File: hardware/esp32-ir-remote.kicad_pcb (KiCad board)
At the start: 2 copper layers, 92 x 44 mm, 57 parts, among them J2 USB_C_Receptacle_USB2.0_14P, J4 GPIO_PWR, J5 EXT_IR, Q3 AO3400A, SW1 RESET, SW2 BOOT, U1 AMS1117-3.3, U3 ESP32-C3-WROOM-02, U4 TSOP382xx, U5 AHT20

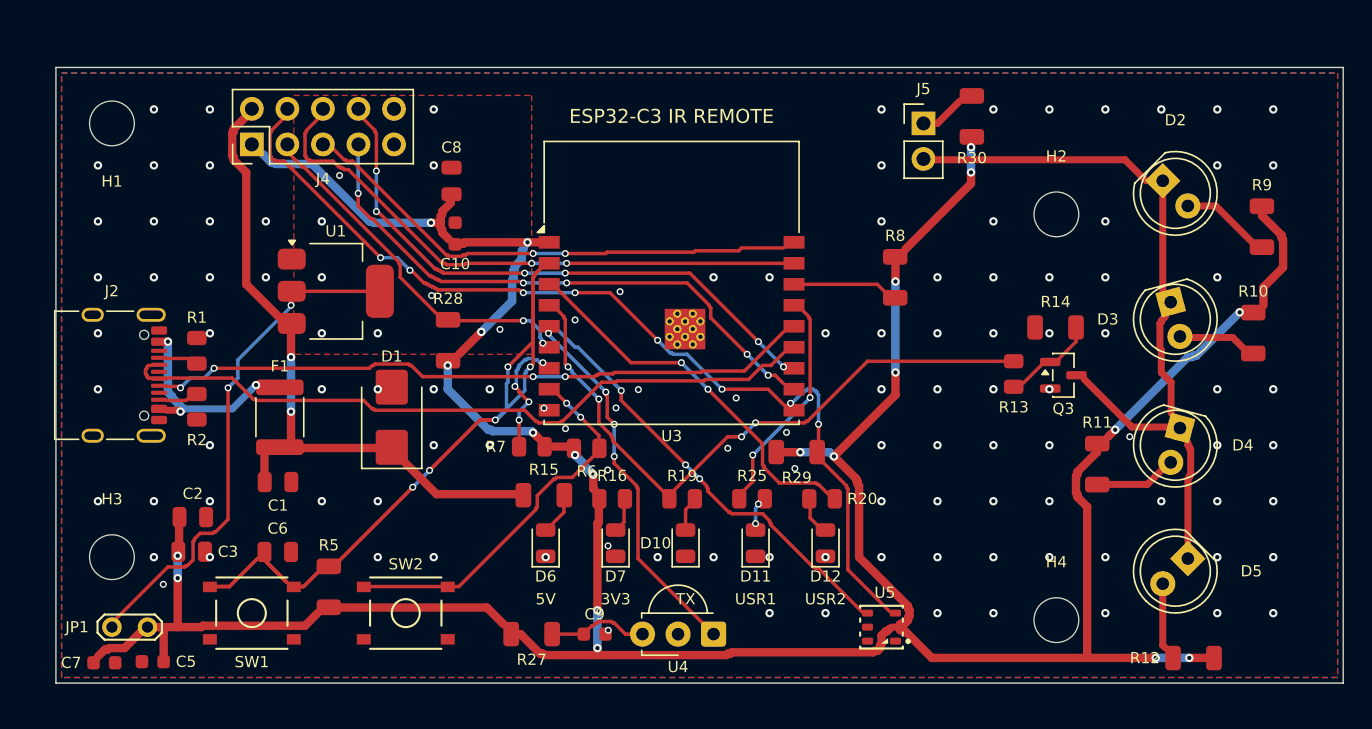
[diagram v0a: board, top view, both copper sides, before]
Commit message: fix(pcb): SI re-layout — USB pair + receiver off the ground plane
Full re-layout pass (Nick's call) resolving the review's SI findings, with
the hand-tuned anchors fixed so the IR fan + U4 south-edge relocation are
preserved (synced into pcb_floorplan.py). Router taught real SI rules:

- pcb_router HARD_F: USB D+/D- forbidden from B.Cu -> both 100% F.Cu, 0 vias,
  no plane crossing (was D+ 5.3mm on B.Cu + 4 vias). SI-critical nets routed
  first so they get clean paths; the USB-C A6<->B6 tie now routes too.
- pcb_router STRONG_F: IR_RX 5.5->2.7mm single crossing; IR_RX_VS 0mm on B.Cu.
- pcb_ldo_pour: /LDO_OUT tab thermal copper ~20 -> ~69mm2.

Result vs committed board (validated on KiCad 10.0.3, libs wired):
  DRC 0 errors; unconnected 1->0; silk_overlap 44->0; silk_over_copper 53->0;
  all 36 multi-pad nets routed; anchors preserved. Baseline refreshed.

Decoupling left ~7mm (bounded by the WROOM module courtyard; module has
internal decoupling). FS-USB skew 12.7mm is electrically irrelevant.
Baseline made on 10.0.3 vs CI's 10.0.2 - watch the first CI run.

https://claude.ai/code/session_012MXcXwLmTqFYpQEkNAaPpq
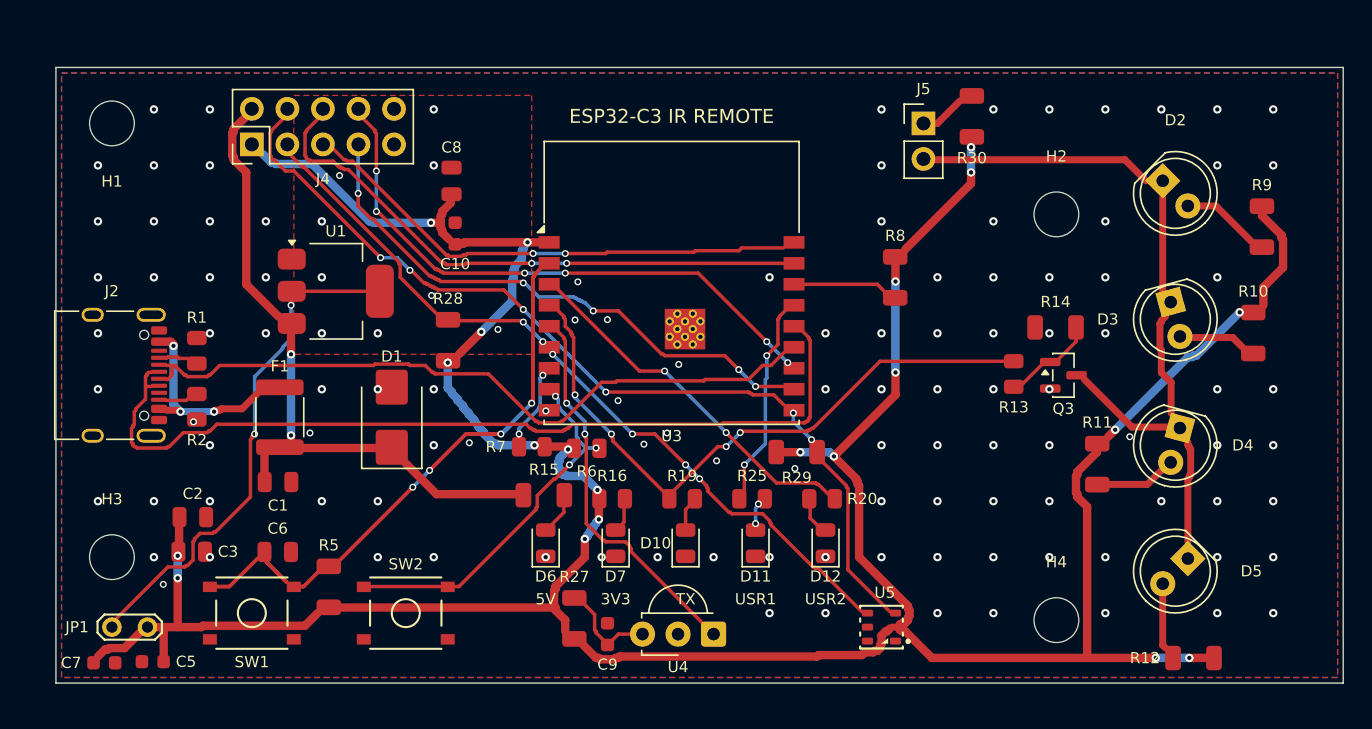
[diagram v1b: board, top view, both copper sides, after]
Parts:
- moved R27 3.25 mm to (143.1, 109.4), turned to 90 degrees
- moved C9 0.92 mm to (145.4, 110.5), turned to 90 degrees
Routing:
- net /USB_D+: track 46.5 -> 62.5 mm, vias 4 -> 0
- net /I2C_SCL: track 65.9 -> 62.3 mm, vias 8 -> 6
- net /IO8_STRAP: track 8.06 -> 5.30 mm, vias 4 -> 2
- net /I2C_SDA: track 55.2 -> 52.4 mm, vias 5 -> 6
- net /ESP_EN: track 70.1 -> 71.8 mm, vias 5 -> 4
- net +3.3V: track 225.5 -> 226.6 mm
- net /USER_LED1: track 15.0 -> 14.0 mm
- net /USER_LED2: track 26.3 -> 25.3 mm
- net /ESP_BOOT: track 23.9 -> 24.6 mm, vias 2 -> 3
- net /IR_RX: track 25.4 -> 25.9 mm, vias 4 -> 2
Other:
- board text added: "2026-06-14 git 68e2410-dirty"
- board text removed: "2026-06-14 git b1f41e0-dirty"

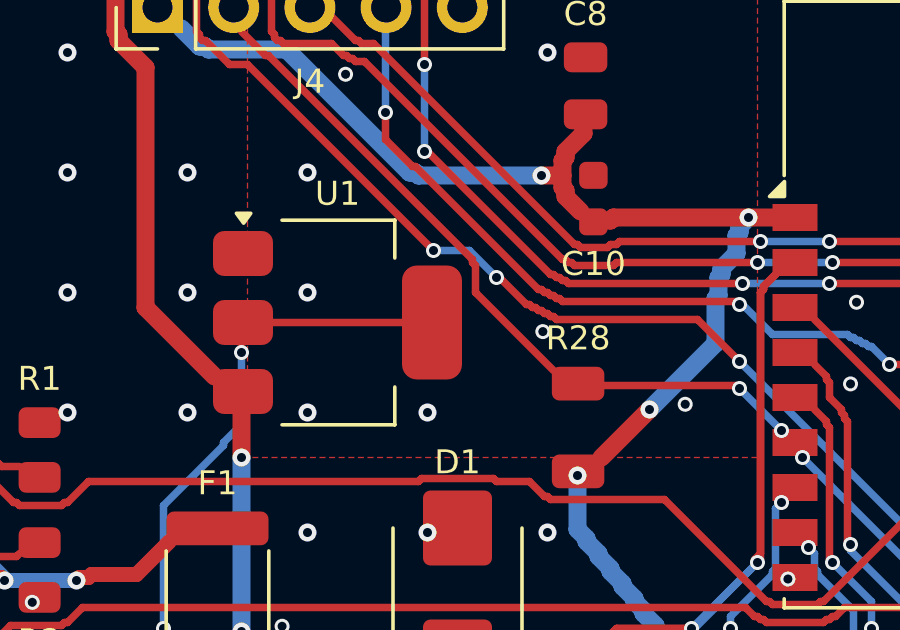
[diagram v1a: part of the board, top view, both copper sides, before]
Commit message: fix(pcb): two-sided LDO thermal stack — B.Cu island + thermal vias
The top-only 68.5 mm2 /LDO_OUT pour left no worst-case margin (T_J ~120 C at
the 0.85 W rated load). pcb_ldo_pour.py now also lays a B.Cu /LDO_OUT island
(43.8 mm2) hugging the tab plus a 2x3 array of thermal vias (0.3/0.6 mm) that
tie the top tab/pour straight through the FR-4 to the bottom island
(~112 mm2 two-sided). The island is kept tight to the tab so the B.Cu ground
plane is only slotted in the west power zone, away from the IR_RX/USB returns.

theta_JA est. ~110 -> ~90 C/W => T_J ~120 -> ~101 C at 25 C ambient (24 C
margin), ~116 C in a 40 C enclosure: now under the 125 C limit at the rated
load. Still short of the 1-in2 ideal (the dense power zone caps the island
size); relocating U1 to open copper is the remaining lever.

Validated on KiCad 10.0.3 in-container: kicad-cli pcb drc 0 violations /
0 unconnected; hardware_validate.py all checks pass, no baseline drift.

https://claude.ai/code/session_01WvC98kUxrLszJZvcojTJeU
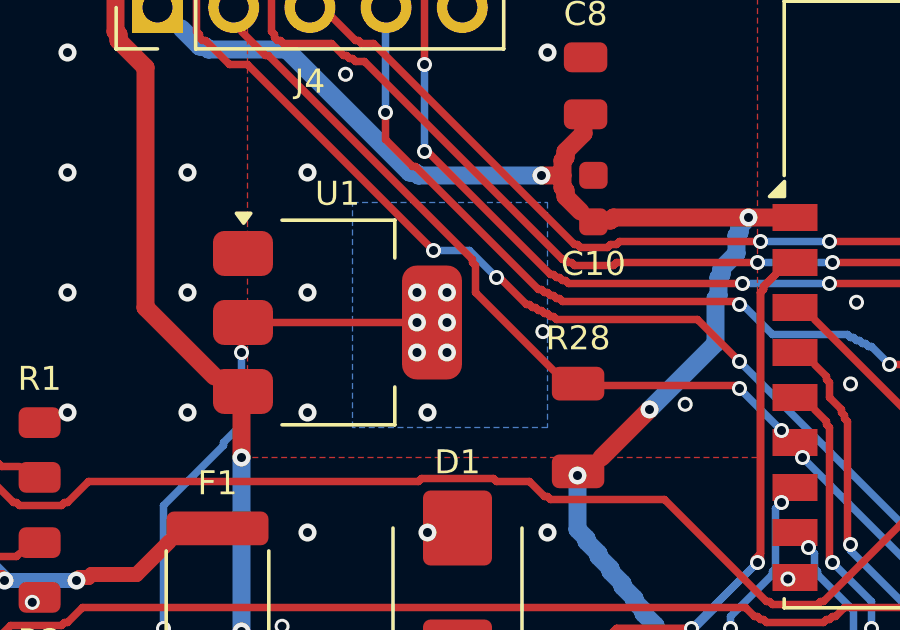
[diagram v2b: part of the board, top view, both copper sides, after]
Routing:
- net /LDO_OUT: vias 2 -> 8
- added copper zone on B.Cu, net /LDO_OUT
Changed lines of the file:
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@@
+	)
+	(via
+		(at 129.65 87)
+		(size 0.6)
+		(drill 0.3)
+		(layers "F.Cu" "B.Cu")
+		(net "/LDO_OUT")
+	)
+	(via
+		(at 128.65 87)
+		(size 0.6)
+		(drill 0.3)
+		(layers "F.Cu" "B.Cu")
+		(net "/LDO_OUT")
 	)
 	(via
@@
 	)
 	(via
+		(at 128.65 86)
+		(size 0.6)
+		(drill 0.3)
+		(layers "F.Cu" "B.Cu")
+		(net "/LDO_OUT")
+	)
+	(via
+		(at 128.65 85)
+		(size 0.6)
+		(drill 0.3)
+		(layers "F.Cu" "B.Cu")
+		(net "/LDO_OUT")
+	)
+	(via
+		(at 129.65 85)
+		(size 0.6)
+		(drill 0.3)
+		(layers "F.Cu" "B.Cu")
+		(net "/LDO_OUT")
+	)
+	(via
 		(at 120.2 96.2)
 		(size 0.5)
+		(drill 0.3)
+		(layers "F.Cu" "B.Cu")
+		(net "/LDO_OUT")
+	)
+	(via
+		(at 129.65 86)
+		(size 0.6)
 		(drill 0.3)
 		(layers "F.Cu" "B.Cu")
@@
 		(layer "F.Cu")
 		(net "Net-(D3-A)")
+	)
+	(zone
+		(net "GND")
+		(layer "F.Cu")
+		(name "gnd_pour_F")
+		(hatch edge 0.5)
+		(connect_pads
+			(clearance 0.3)
+		)
+		(min_thickness 0.2)
+		(fill yes
+			(thermal_gap 0.3)
+			(thermal_bridge_width 0.5)
+			(island_removal_mode 2)
+			(island_area_min 2)
+		)
+		(polygon
+			(pts
+				(xy 106.4 70.4) (xy 197.6 70.4) (xy 197.6 113.6) (xy 106.4 113.6)
+			)
+		)
 	)
 	(zone
@@
 			(pts
 				(xy 123 72) (xy 140 72) (xy 140 90.5) (xy 123 90.5)
-			)
-		)
-	)
-	(zone
-		(net "GND")
-		(layer "F.Cu")
-		(name "gnd_pour_F")
-		(hatch edge 0.5)
-		(connect_pads
-			(clearance 0.3)
-		)
-		(min_thickness 0.2)
-		(fill yes
-			(thermal_gap 0.3)
-			(thermal_bridge_width 0.5)
-			(island_removal_mode 2)
-			(island_area_min 2)
-		)
-		(polygon
-			(pts
-				(xy 106.4 70.4) (xy 197.6 70.4) (xy 197.6 113.6) (xy 106.4 113.6)
 			)
 		)
@@
 			)
 		)
+	)
+	(zone
+		(net "/LDO_OUT")
+		(layer "B.Cu")
+		(name "LDO_OUT_thermal_btm")
+		(hatch edge 0.5)
+		(priority 1)
+		(connect_pads yes
+			(clearance 0.3)
+		)
+		(min_thickness 0.2)
+		(fill yes
+			(thermal_gap 0.5)
+			(thermal_bridge_width 0.5)
+			(island_removal_mode 0)
+		)
+		(polygon
+			(pts
+				(xy 126.5 82) (xy 133 82) (xy 133 89.5) (xy 126.5 89.5)
+			)
+		)

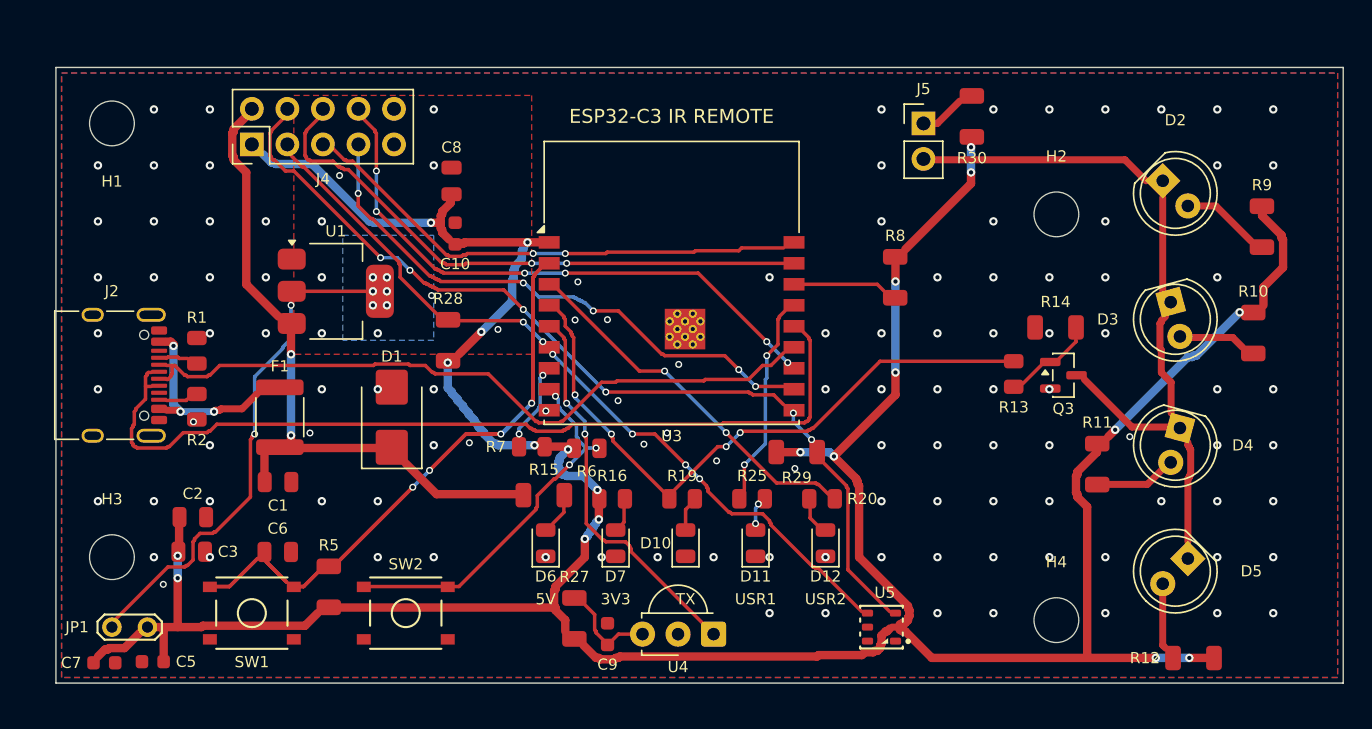
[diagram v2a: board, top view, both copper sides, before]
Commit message: feat(pcb): FreeRouting routes the board clean; retire home-grown router
Wire FreeRouting in as the ROUTE stage and route the real board with it. The
hand-rolled greedy A* router + rip-up finisher could never place the congested
module-west escape cleanly (one net always frozen out, finisher left dangling
stubs / co-located vias / mangled neighbours). FreeRouting's negotiated
rip-up-and-reroute routes all 127 nets to 0 unrouted in ~7s.

Pipeline ROUTE stage: pcb_router.py + pcb_finish.py  ->  pcb_route_fr.py
(ExportSpecctraDSN -> freerouting 2.2.4 -> ImportSpecctraSES). New pipeline:
floorplan -> place -> rip -> route_fr -> pour -> ldo_pour -> silk.

Results (full hardware_validate.py gate, KiCad 10.0.3):
  - 0 unconnected, parity 19, all checks PASS.
  - No antenna-keepout intrusion, no dangling/duplicate vias.
  - LDO thermal: U1 in the NW corner, rot90 (SOT-223 tab faces N into a
    257 mm^2 to-the-edge pour that displaces GND); T_J ~75 C at 0.85 W.
  - FreeRouting run is byte-for-bit deterministic (-mt 1 -is sequential
    -us greedy, pinned jar) — verified md5-identical .ses across runs, so the
    committed board regenerates exactly.

GND: kept FR's GND routing (dropping it strands pads the pour can't reach where
USB sits on B.Cu) + GND pour as the plane; pcb_route_fr drops the few GND traces
FR runs to the board edge; pcb_pour removes unconnected GND islands (ALWAYS).

Retire pcb_router.py + pcb_finish.py (in git history). Rationale, determinism,
and optional refinements (USB->F.Cu; pour-only GND) in
hardware/notes/autorouting-freerouting.md. ROADMAP updated.

https://claude.ai/code/session_01WvC98kUxrLszJZvcojTJeU
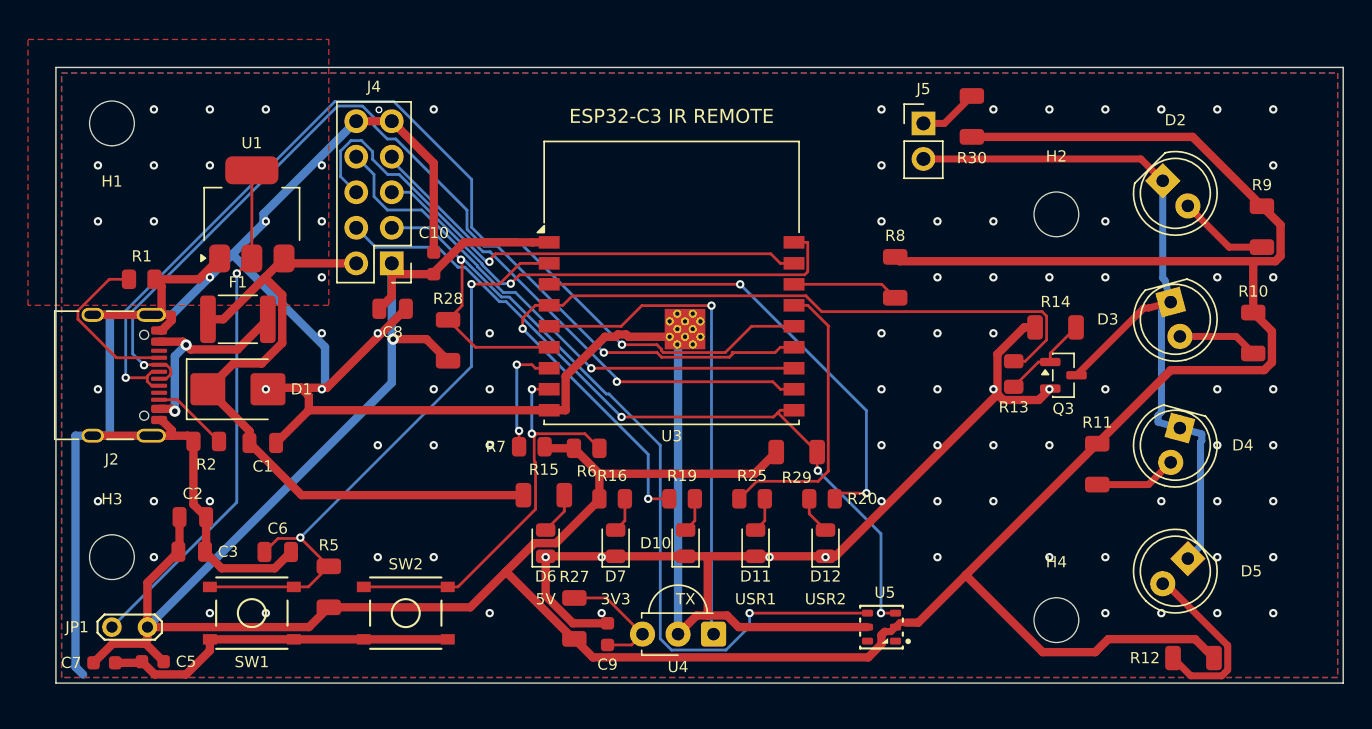
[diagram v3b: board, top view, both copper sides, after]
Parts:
- moved J4 13.1 mm to (130.0, 84.0), turned to 180 degrees
- moved D1 11.2 mm to (119.0, 93.0), turned to 0 degrees
- moved C8 10.1 mm to (130.1, 87.2), turned to 0 degrees
- moved U1 8.14 mm to (120.0, 80.5), turned to 90 degrees
- moved F1 7.62 mm to (119.0, 88.0), turned to 0 degrees
- moved R1 6.45 mm to (112.1, 85.1), turned to 0 degrees
- moved C1 3.00 mm to (120.8, 96.8)
- moved C10 2.62 mm to (133.0, 84.0)
- moved R2 2.57 mm to (116.7, 96.7), turned to 0 degrees
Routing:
- net GND: track 0.00 -> 292.2 mm, vias 120 -> 90
- net +3.3V: track 226.6 -> 275.7 mm, vias 21 -> 1
- net /ESP_EN: track 71.8 -> 44.3 mm, vias 4 -> 2
- net /USB_D-: track 49.8 -> 69.9 mm, vias 0 -> 2
- net /IR_TX: track 43.4 -> 61.5 mm, vias 4 -> 2
- net /I2C_SDA: track 52.4 -> 69.2 mm, vias 6 -> 2
- net /IR_DRAIN: track 44.5 -> 56.8 mm
- net +5V: track 39.0 -> 50.6 mm, vias 2 -> 0
- net Net-(J2-CC1): track 1.58 -> 12.1 mm
- net /USB_D+: track 62.5 -> 72.9 mm, vias 0 -> 2
- net /IR_RX: track 25.9 -> 35.8 mm, vias 2 -> 1
- net /USER_LED2: track 25.3 -> 34.7 mm
- net Net-(D5-A): track 3.88 -> 12.8 mm
- net /I2C_SCL: track 62.3 -> 55.5 mm, vias 6 -> 3
- net /USER_LED1: track 14.0 -> 20.6 mm, vias 2 -> 0
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- removed copper zone on B.Cu, net /LDO_OUT
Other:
- board text added: "2026-06-15 git 92c3a90-dirty"
- board text removed: "2026-06-14 git 68e2410-dirty"

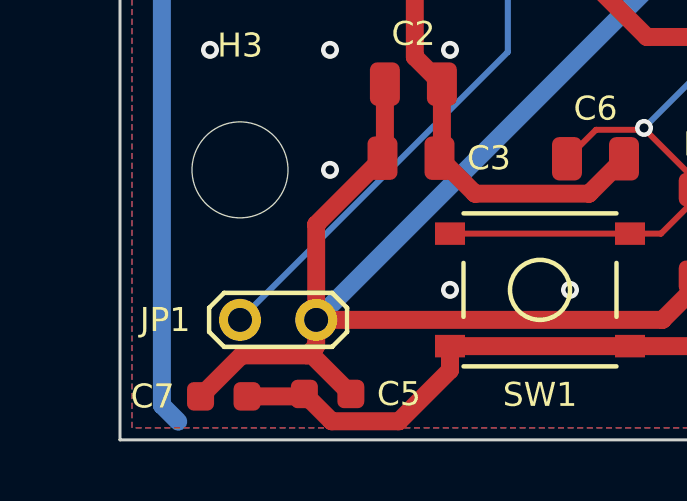
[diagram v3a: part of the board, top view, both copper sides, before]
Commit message: hw: remove JP1 LDO-disconnect jumper — single-supply 3V3 rail
The series jumper on the LDO output is deleted; the AMS1117 VO now drives
+3.3V directly. Isolating the LDO (for bench injection or a battery
prototype) is done by desoldering the SOT-223 instead — the jumper's rare
benefit didn't justify its cost (the open-jumper state left the LDO output
with no stability cap, and split the node C2/C3 want to sit on). A real
second supply needs an OR-ing front end, not a rail tap; deferred to a
later rev.

Schematic: drop JP1 + its label/wire stubs, collapse /LDO_OUT into +3.3V,
remove the now-redundant +3.3V PWR_FLAG (it caused a power-output↔
power-output ERC conflict once the regulator drives the net). ERC clean.

PCB: remove JP1 footprint, re-net the 5 /LDO_OUT copper objects to +3.3V,
add 2 stitching vias at the old JP1 pad sites (the THT TestPoint pads had
been bridging F.Cu↔B.Cu) + a short F.Cu bridge across the gap; re-pour GND
and the LDO thermal pour (now +3.3V, 257mm² bonded to the tab). DRC 0/0.

Validators: golden_netlist_v2 (LDO_OUT row dropped), hardware_validate
polarity (U1.2=+3.3V) + LCSC allowlist, ci-baseline drc_parity 21->19.
hardware_validate EXIT 0.

Docs: rewrite power-supply.md v1->v2 (was still describing the AP63203
buck); add a layer-policy section to layout.md (signal-on-F.Cu /
power-takes-short-B.Cu-dips, + autorouter-ruleset findings). CLAUDE.md:
record that KiCad is installable in remote sessions (with the python3.12
add-apt-repository workaround), not Mac-only.

https://claude.ai/code/session_016mTYyBymU4FS9LKdtfpLwm
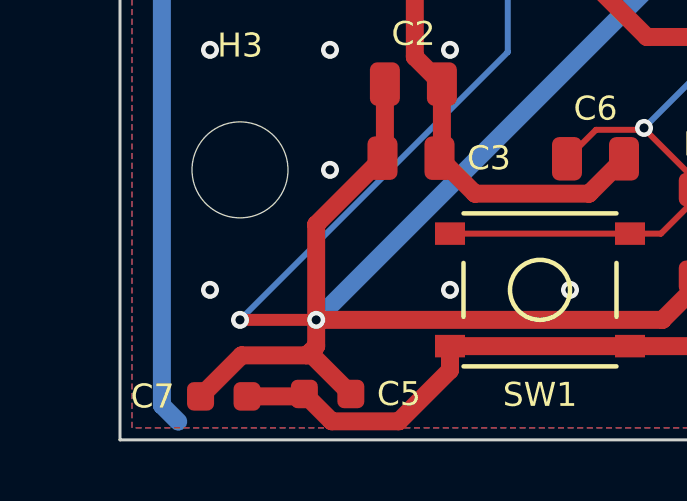
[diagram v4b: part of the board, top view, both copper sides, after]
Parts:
- removed JP1: LDO Disable, TestPoint:TestPoint_2Pads_Pitch2.54mm_Drill0.8mm
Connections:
- U1 pad 2: /LDO_OUT -> +3.3V
- U5 pad 1: (no net) -> unconnected-(U5-NC-Pad1)
- U5 pad 6: (no net) -> unconnected-(U5-NC-Pad6)
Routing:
- net +3.3V: track 275.7 -> 315.1 mm, vias 1 -> 4
- net /LDO_OUT: track 36.8 -> 0.00 mm, vias 1 -> 0
- net GND: vias 90 -> 91
- added copper zone on F.Cu, net +3.3V
- removed copper zone on F.Cu, net /LDO_OUT
